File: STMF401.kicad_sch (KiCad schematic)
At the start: 21 parts, among them J6 Conn_01x04_Pin, U7 STM32F407VETx, U8 AT24C256, Y1 X322525MQB4SI

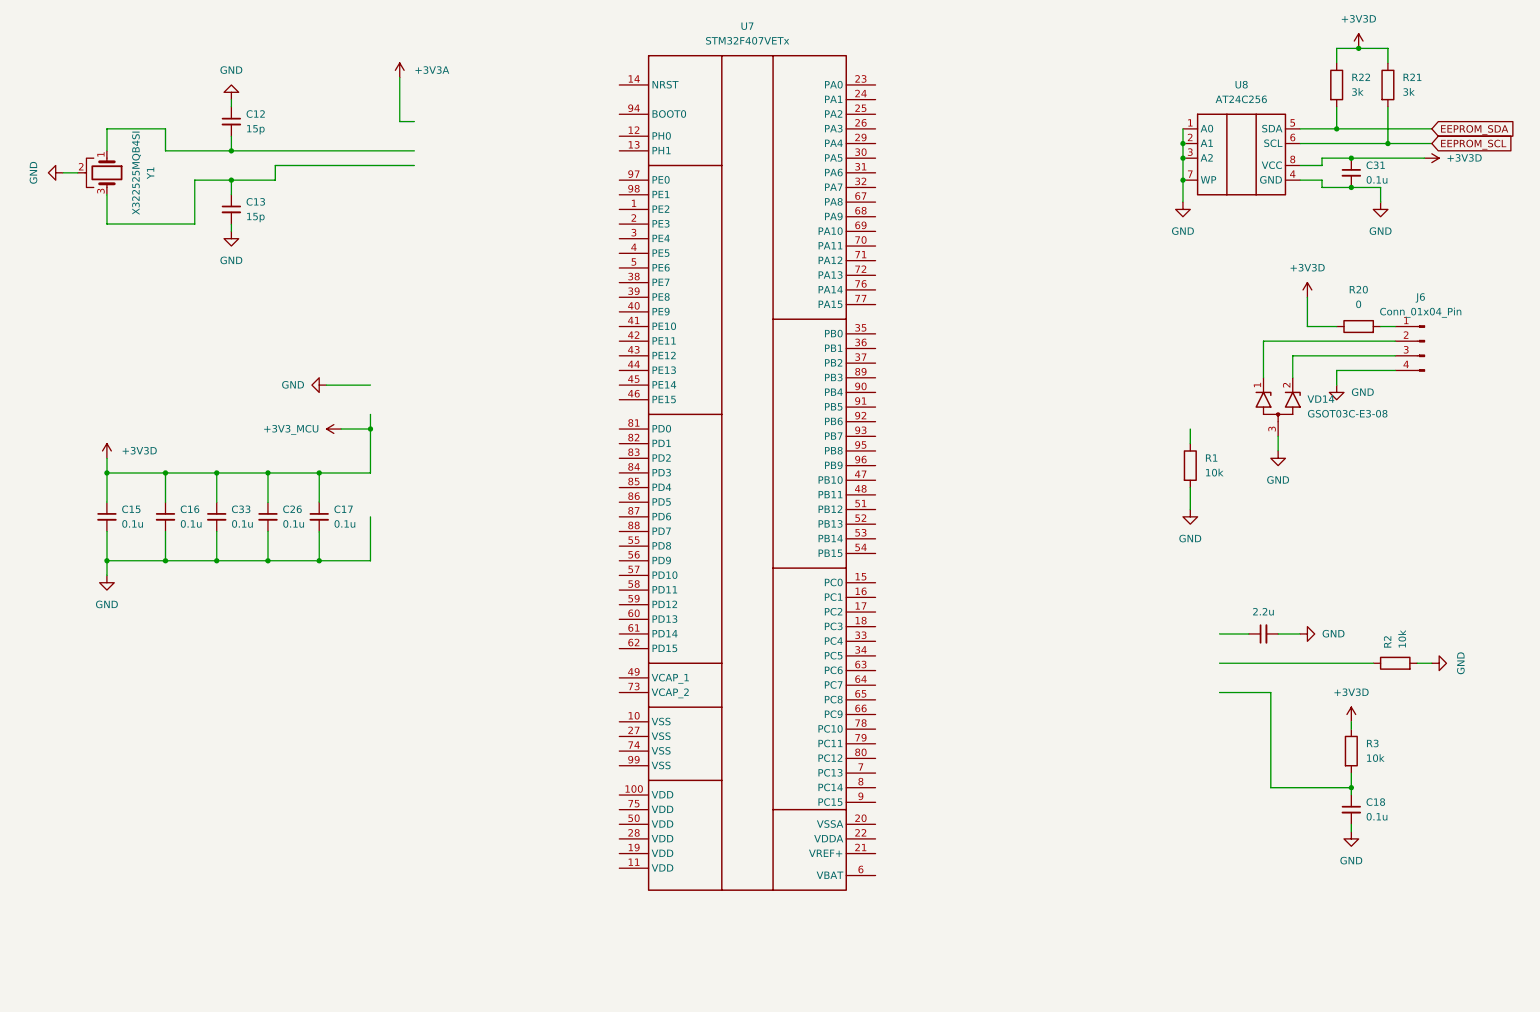
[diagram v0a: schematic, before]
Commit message: feat: добавлены все элементы схемы, начал соединение сигнгальных линий к микроконтроллеру
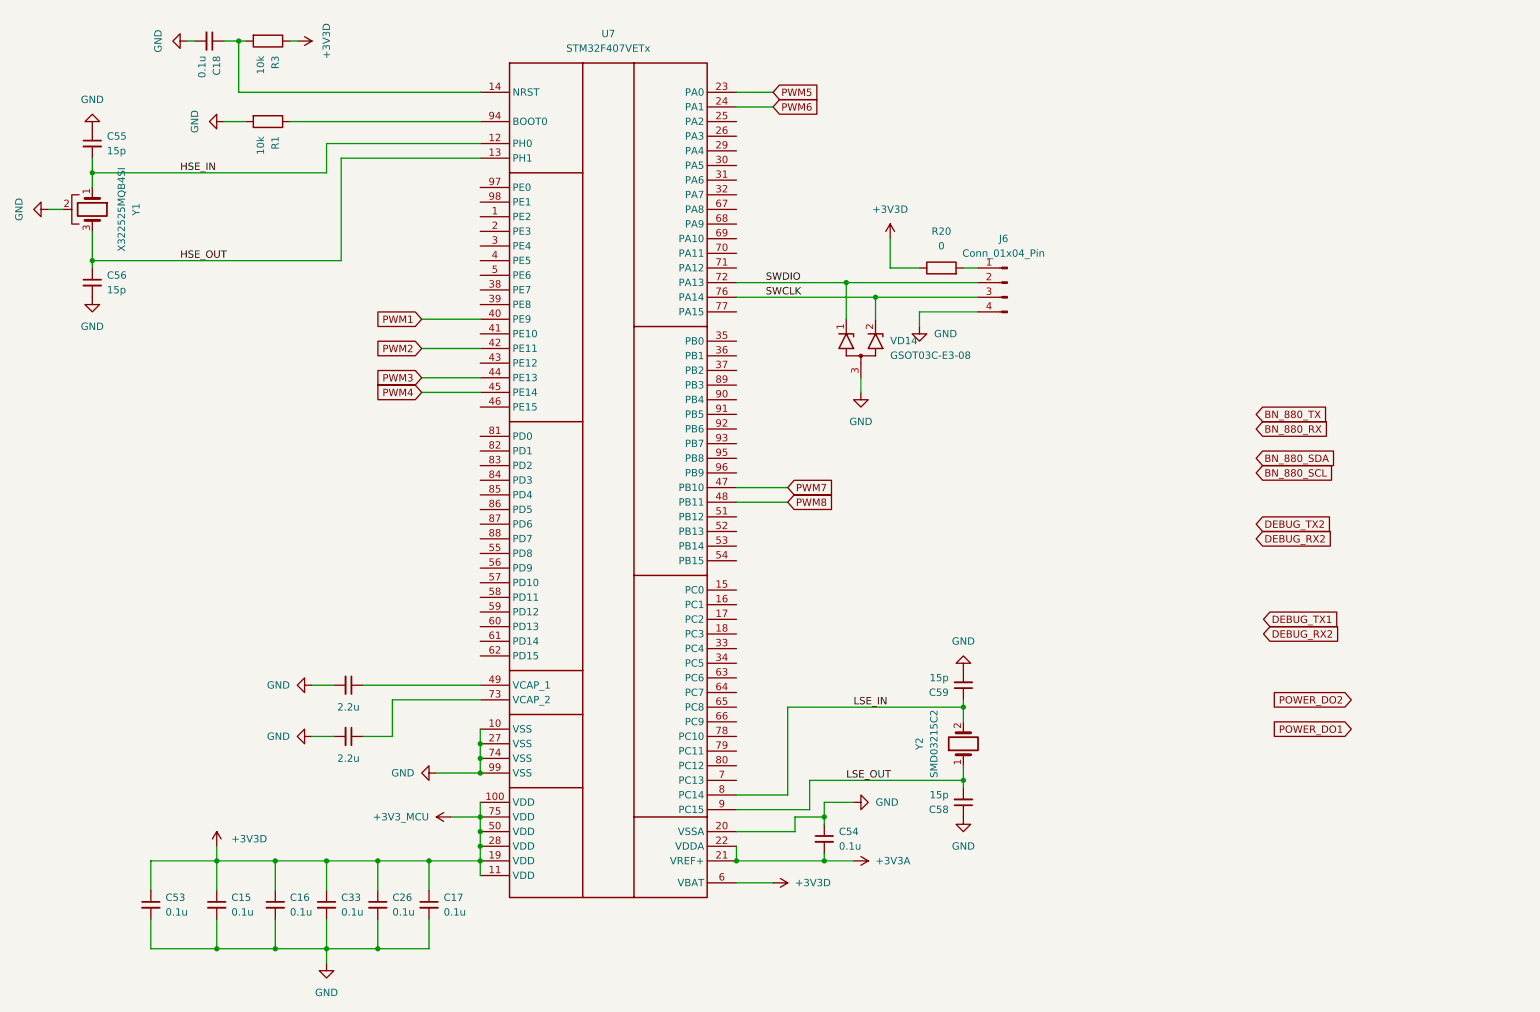
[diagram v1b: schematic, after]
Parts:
- removed C12, C13: 15p, Capacitor_SMD:C_0805_2012Metric_Pad1.18x1.45mm_HandSolder, symbol Device:C_Small
- removed C31: 0.1u, Capacitor_SMD:C_0805_2012Metric_Pad1.18x1.45mm_HandSolder, symbol Device:C_Small
- removed R2: 10k, Resistor_SMD:R_0805_2012Metric_Pad1.20x1.40mm_HandSolder, symbol Device:R
- removed R21, R22: 3k, Resistor_SMD:R_0805_2012Metric_Pad1.20x1.40mm_HandSolder, symbol Device:R
- removed U8: AT24C256, Package_SO:SOIC-8_3.9x4.9mm_P1.27mm, symbol EEPROM:AT24C256
- added C53, C54: 0.1u, Capacitor_SMD:C_0805_2012Metric_Pad1.18x1.45mm_HandSolder, symbol Device:C_Small
- added C55, C56, C58, C59: 15p, Capacitor_SMD:C_0805_2012Metric_Pad1.18x1.45mm_HandSolder, symbol Device:C_Small
- added C57: 2.2u, Capacitor_SMD:C_0805_2012Metric_Pad1.18x1.45mm_HandSolder, symbol Device:C_Small
- added Y2: SMD03215C2, Crystal:Crystal_SMD_3215-2Pin_3.2x1.5mm, symbol Oscillators:X322525MQB4SI
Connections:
- net +3V3A: now also U7.21 (VREF+), U7.22 (VDDA), C54.2
- net +3V3D: now also U7.100 (VDD), U7.11 (VDD), U7.19 (VDD), U7.28 (VDD), U7.50 (VDD), U7.6 (VBAT), U7.75 (VDD), C53.1
- net GND: now also U7.10 (VSS), U7.20 (VSSA), U7.27 (VSS), U7.74 (VSS), U7.99 (VSS), C53.2, C54.1, C55.1, C56.2, C57.2, C58.1, C59.2
- net HSE_IN: now reaches Y1.1 (OSC)
- net HSE_IN: now also U7.12 (PH0), C55.2
- net HSE_OUT: now reaches Y1.3 (OSC)
- net HSE_OUT: now also U7.13 (PH1), C56.1
- net at C18.1, R3.2: now also U7.14 (NRST)
- net SWDIO: now reaches J6.2 (Pin_2), VD14.1 (K1)
- net SWDIO: now also U7.72 (PA13)
- net SWCLK: now reaches J6.3 (Pin_3), VD14.2 (K2)
- net SWCLK: now also U7.76 (PA14)
- net at R1.1: now also U7.94 (BOOT0)
- net PWM5: now reaches U7.23 (PA0)
- net PWM6: now reaches U7.24 (PA1)
- net PWM1: now reaches U7.40 (PE9)
- net PWM2: now reaches U7.42 (PE11)
- net PWM3: now reaches U7.44 (PE13)
- net PWM4: now reaches U7.45 (PE14)
- net PWM7: now reaches U7.47 (PB10)
- net PWM8: now reaches U7.48 (PB11)
- net at U7.49 (VCAP_1): now also C19.1
- net at U7.73 (VCAP_2): now also C57.1
- net LSE_IN: now reaches U7.8 (PC14)
- net LSE_IN: now also C59.1, Y2.2 (OSC)
- net LSE_OUT: now reaches U7.9 (PC15)
- net LSE_OUT: now also C58.2, Y2.1 (OSC)
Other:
- moved on the sheet: C15, C16, C17, C18, C26, C33, J6, R1, R20, R3, U7, VD14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

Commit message: feat: проведены все внешние линии и лдини связи с модулями LoRa
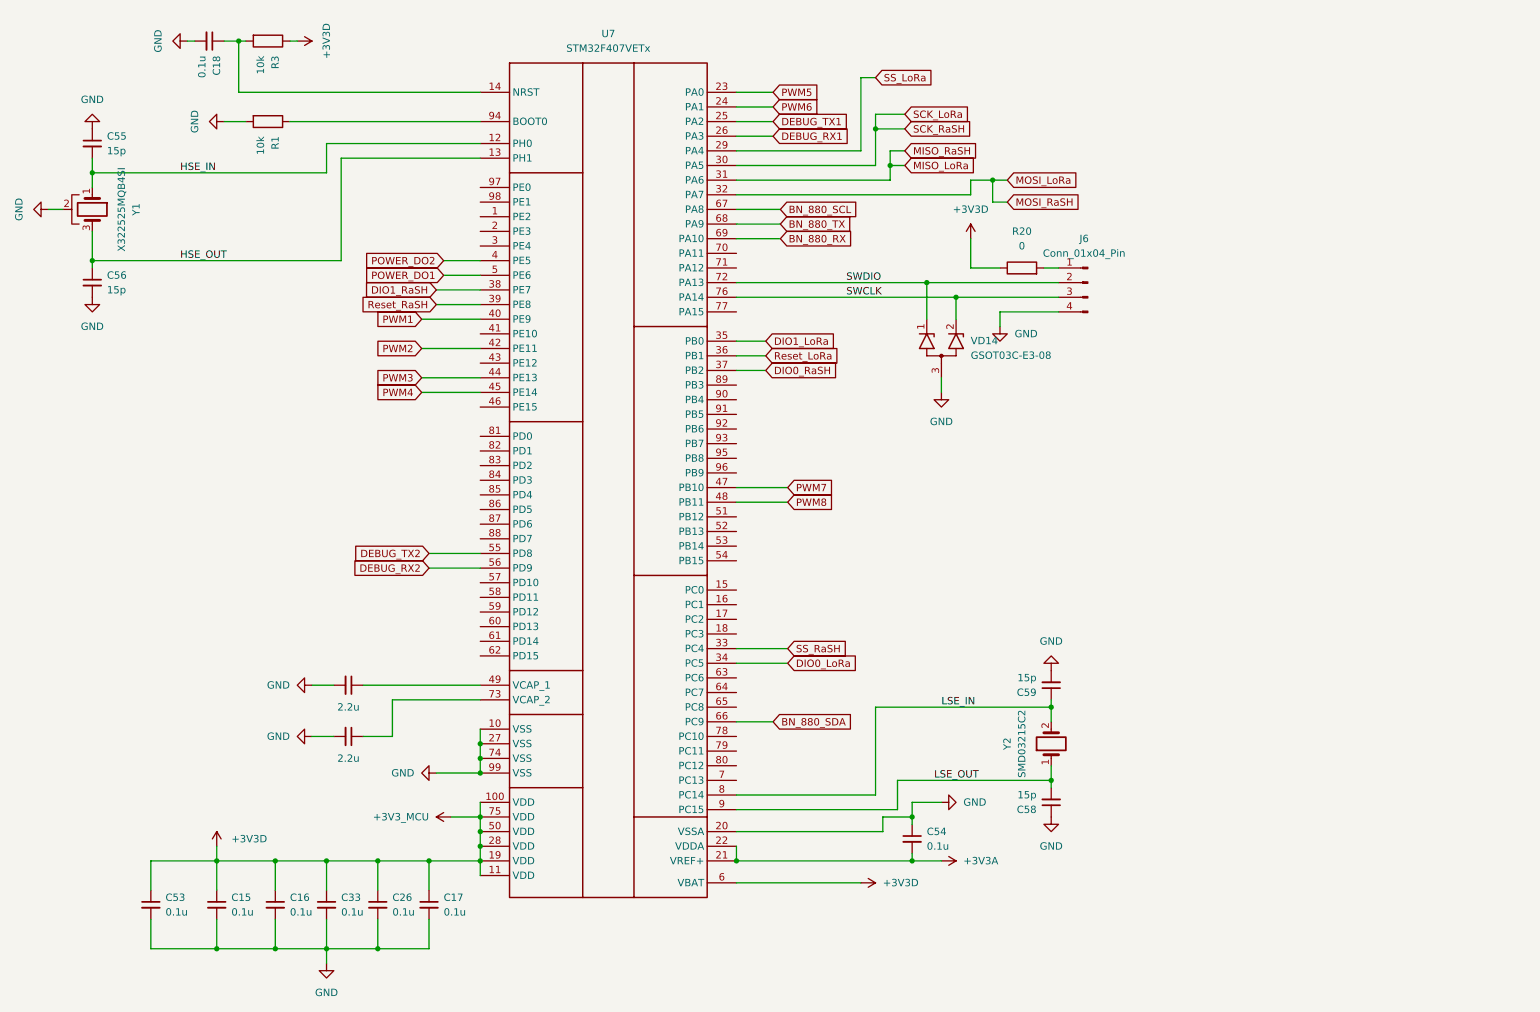
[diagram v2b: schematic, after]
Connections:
- net BN_880_RX: now also U7.69 (PA10)
- net BN_880_SCL: now also U7.67 (PA8)
- net BN_880_SDA: now also U7.66 (PC9)
- net BN_880_TX: now also U7.68 (PA9)
- net DEBUG_RX2: now also U7.56 (PD9)
- net DEBUG_TX1: now also U7.25 (PA2)
- net DEBUG_TX2: now also U7.55 (PD8)
- net POWER_DO1: now also U7.5 (PE6)
- net POWER_DO2: now also U7.4 (PE5)
- net DEBUG_RX1: now reaches U7.26 (PA3)
- net SS_LoRa: now reaches U7.29 (PA4)
- net SCK_LoRa: now reaches U7.30 (PA5)
- net MISO_LoRa: now reaches U7.31 (PA6)
- net MOSI_LoRa: now reaches U7.32 (PA7)
- net SS_RaSH: now reaches U7.33 (PC4)
- net DIO0_LoRa: now reaches U7.34 (PC5)
- net DIO1_LoRa: now reaches U7.35 (PB0)
- net Reset_LoRa: now reaches U7.36 (PB1)
- net DIO0_RaSH: now reaches U7.37 (PB2)
- net DIO1_RaSH: now reaches U7.38 (PE7)
- net Reset_RaSH: now reaches U7.39 (PE8)
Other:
- moved on the sheet: C54, C58, C59, J6, R20, VD14, Y2

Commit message: feat: добавлены все сигнальные линии к МК
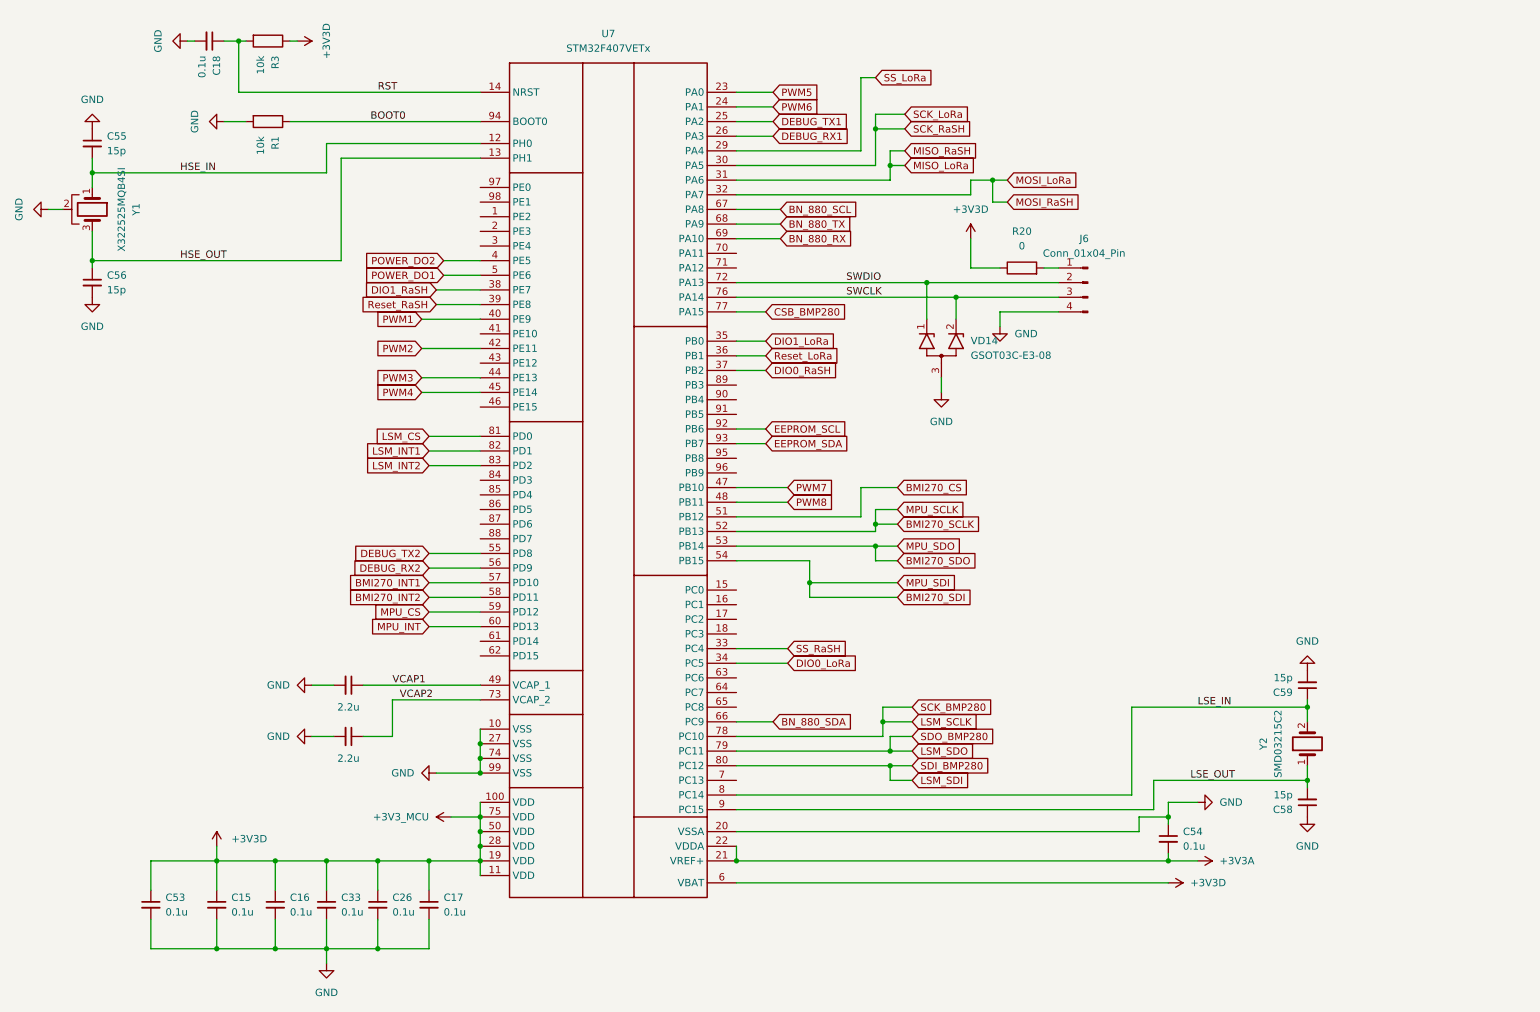
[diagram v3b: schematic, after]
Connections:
- net RST: now reaches C18.1, R3.2, U7.14 (NRST)
- net VCAP2: now reaches C57.1, U7.73 (VCAP_2)
- net BOOT0: now reaches R1.1, U7.94 (BOOT0)
- net VCAP1: now reaches C19.1, U7.49 (VCAP_1)
- net BMI270_CS: now reaches U7.51 (PB12)
- net BMI270_SCLK: now reaches U7.52 (PB13)
- net BMI270_SDO: now reaches U7.53 (PB14)
- net BMI270_SDI: now reaches U7.54 (PB15)
- net BMI270_INT1: now reaches U7.57 (PD10)
- net BMI270_INT2: now reaches U7.58 (PD11)
- net MPU_CS: now reaches U7.59 (PD12)
- net MPU_INT: now reaches U7.60 (PD13)
- net CSB_BMP280: now reaches U7.77 (PA15)
- net LSM_SCLK: now reaches U7.78 (PC10)
- net LSM_SDO: now reaches U7.79 (PC11)
- net LSM_SDI: now reaches U7.80 (PC12)
- net LSM_CS: now reaches U7.81 (PD0)
- net LSM_INT1: now reaches U7.82 (PD1)
- net LSM_INT2: now reaches U7.83 (PD2)
- net EEPROM_SCL: now reaches U7.92 (PB6)
- net EEPROM_SDA: now reaches U7.93 (PB7)
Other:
- moved on the sheet: C54, C58, C59, Y2

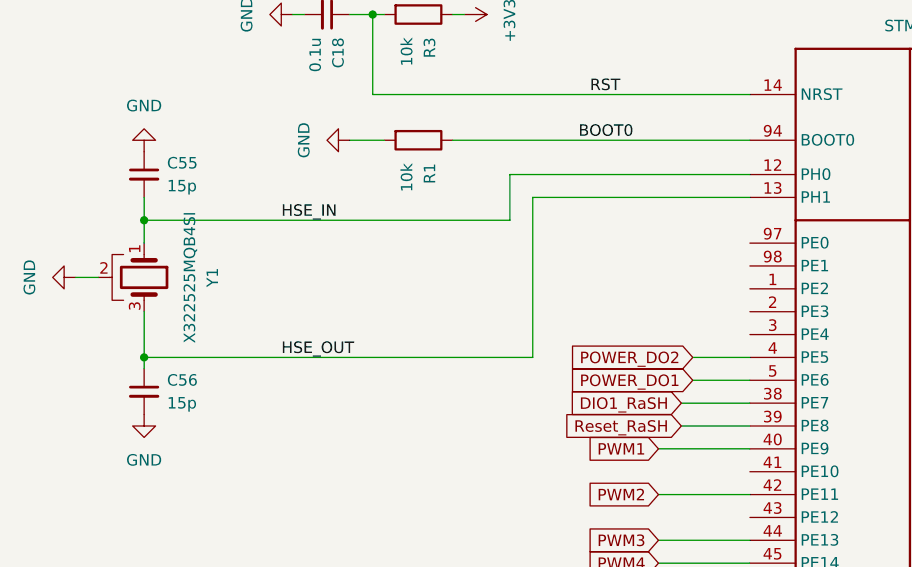
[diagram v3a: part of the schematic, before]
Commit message: feat: добавлены светодиоды, размещены почти все компоненты кроме модулей IMU
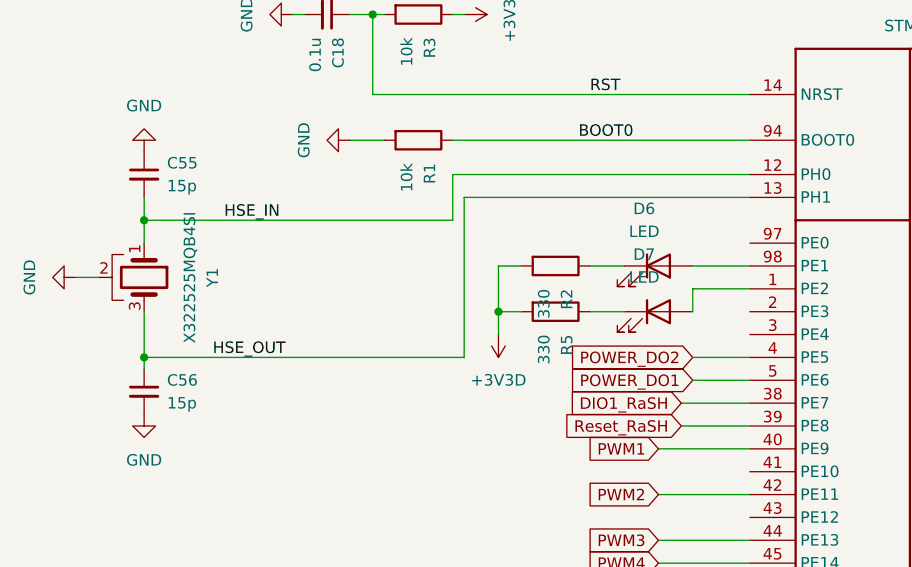
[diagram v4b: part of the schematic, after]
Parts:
- added D6, D7: LED, LED_SMD:LED_0805_2012Metric_Pad1.15x1.40mm_HandSolder, symbol Device:LED
- added R2, R5: 330, Resistor_SMD:R_0805_2012Metric_Pad1.20x1.40mm_HandSolder, symbol Device:R
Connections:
- net +3V3D: now also R2.2, R5.2
- net at U7.1 (PE2): now also D7.2 (A)
- net at U7.98 (PE1): now also D6.2 (A)
- new net: D6.1 (K), R2.1
- new net: D7.1 (K), R5.1
